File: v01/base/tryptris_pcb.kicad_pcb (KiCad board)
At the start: 2 copper layers, 298.8 x 122 mm, 143 parts, among them J1 USB_C_Receptacle_USB2.0, J2 I2C-L, J3 I2C-R, J4 AVR-ISP-6, SW1 Reset, U1 ATmega32U4-AU, U2 MCP23017_SO, U3 PRTR5V0U2X, U4 HOLE, Y1 16Mhz

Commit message: Tweak routing more.
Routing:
- net Col1: track 214.3 -> 213.0 mm
- net Row1-L: track 154.8 -> 154.3 mm

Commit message: Add copper fills to base.
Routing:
- net Row2-R: track 129.3 -> 133.9 mm
- net Row3-R: track 146.9 -> 150.6 mm
- net Row4-R: track 107.3 -> 111.0 mm
- net +5V: track 205.3 -> 207.6 mm
- net Col0: track 239.0 -> 240.5 mm
- net Row1-L: track 154.3 -> 152.9 mm
- net Row3-L: track 152.1 -> 151.5 mm
- net VSS: vias 0 -> 4
- net GND: vias 2 -> 13

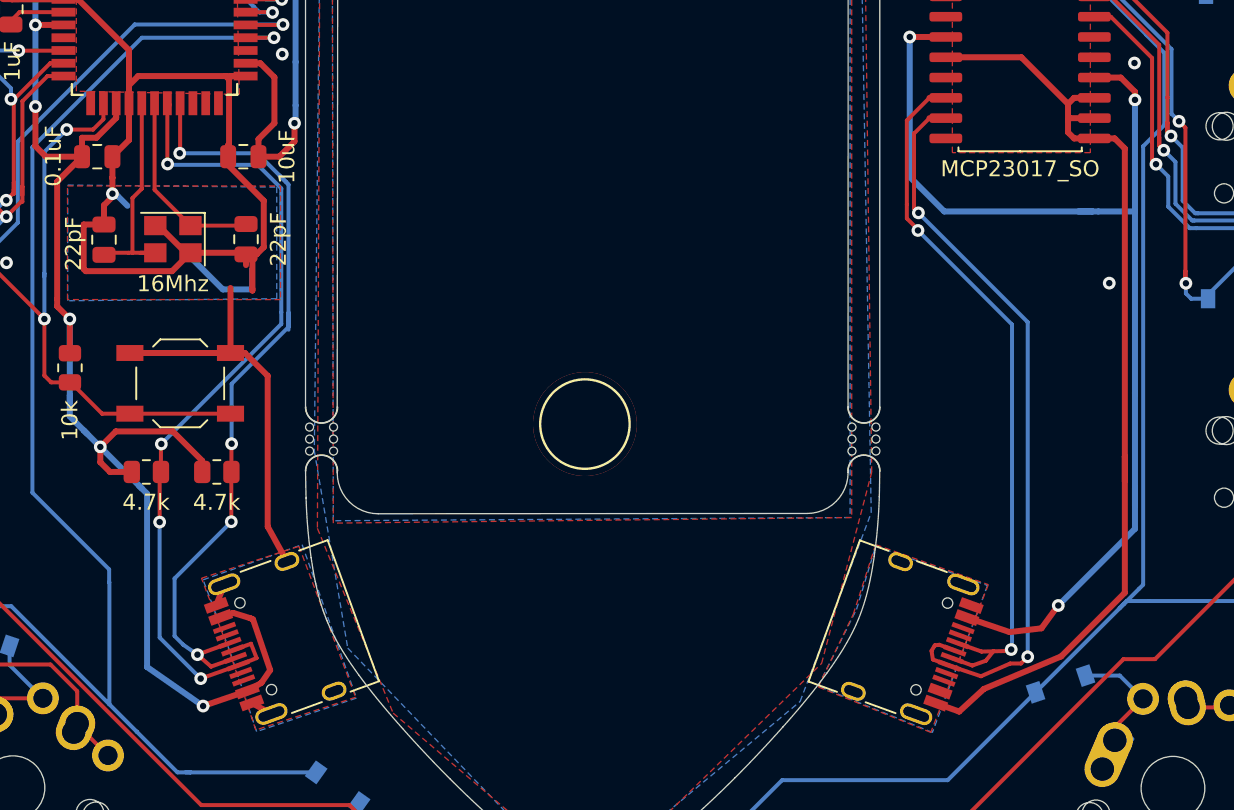
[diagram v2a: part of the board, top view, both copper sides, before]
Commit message: Add interconnect ESD to base.
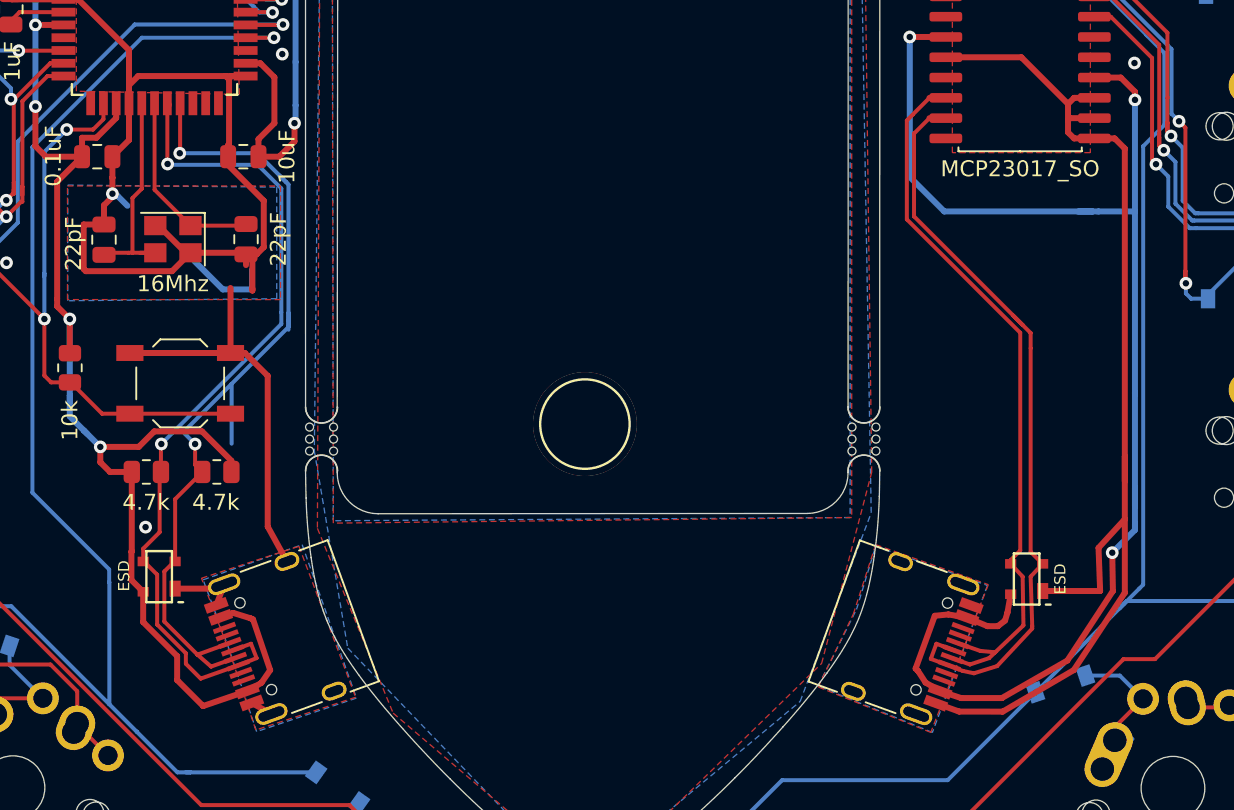
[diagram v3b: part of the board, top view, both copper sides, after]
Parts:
- added U4: PRTR5V0U2X, Keebio-Parts:SOT-143B, F.Cu at (148.8, 111.2)
- added U5: PRTR5V0U2X, Keebio-Parts:SOT-143B, F.Cu at (203.2, 111.4)
- turned R7 to 180 degrees
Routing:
- net VBUS: track 71.8 -> 89.1 mm
- net VSS: track 61.9 -> 71.4 mm, vias 4 -> 3
- net SDA-L: track 50.4 -> 55.6 mm, vias 4 -> 2
- net GND: track 194.2 -> 197.4 mm, vias 13 -> 14
- net SDA-R: track 46.8 -> 48.4 mm, vias 2 -> 0
- net +5V: track 207.6 -> 206.4 mm, vias 9 -> 8
- net SCL-R: track 45.4 -> 46.0 mm, vias 2 -> 0
- net SCL-L: track 53.1 -> 53.7 mm, vias 4 -> 2
